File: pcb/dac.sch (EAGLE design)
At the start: 10 parts, among them U1 PIC16F1773-I/SP

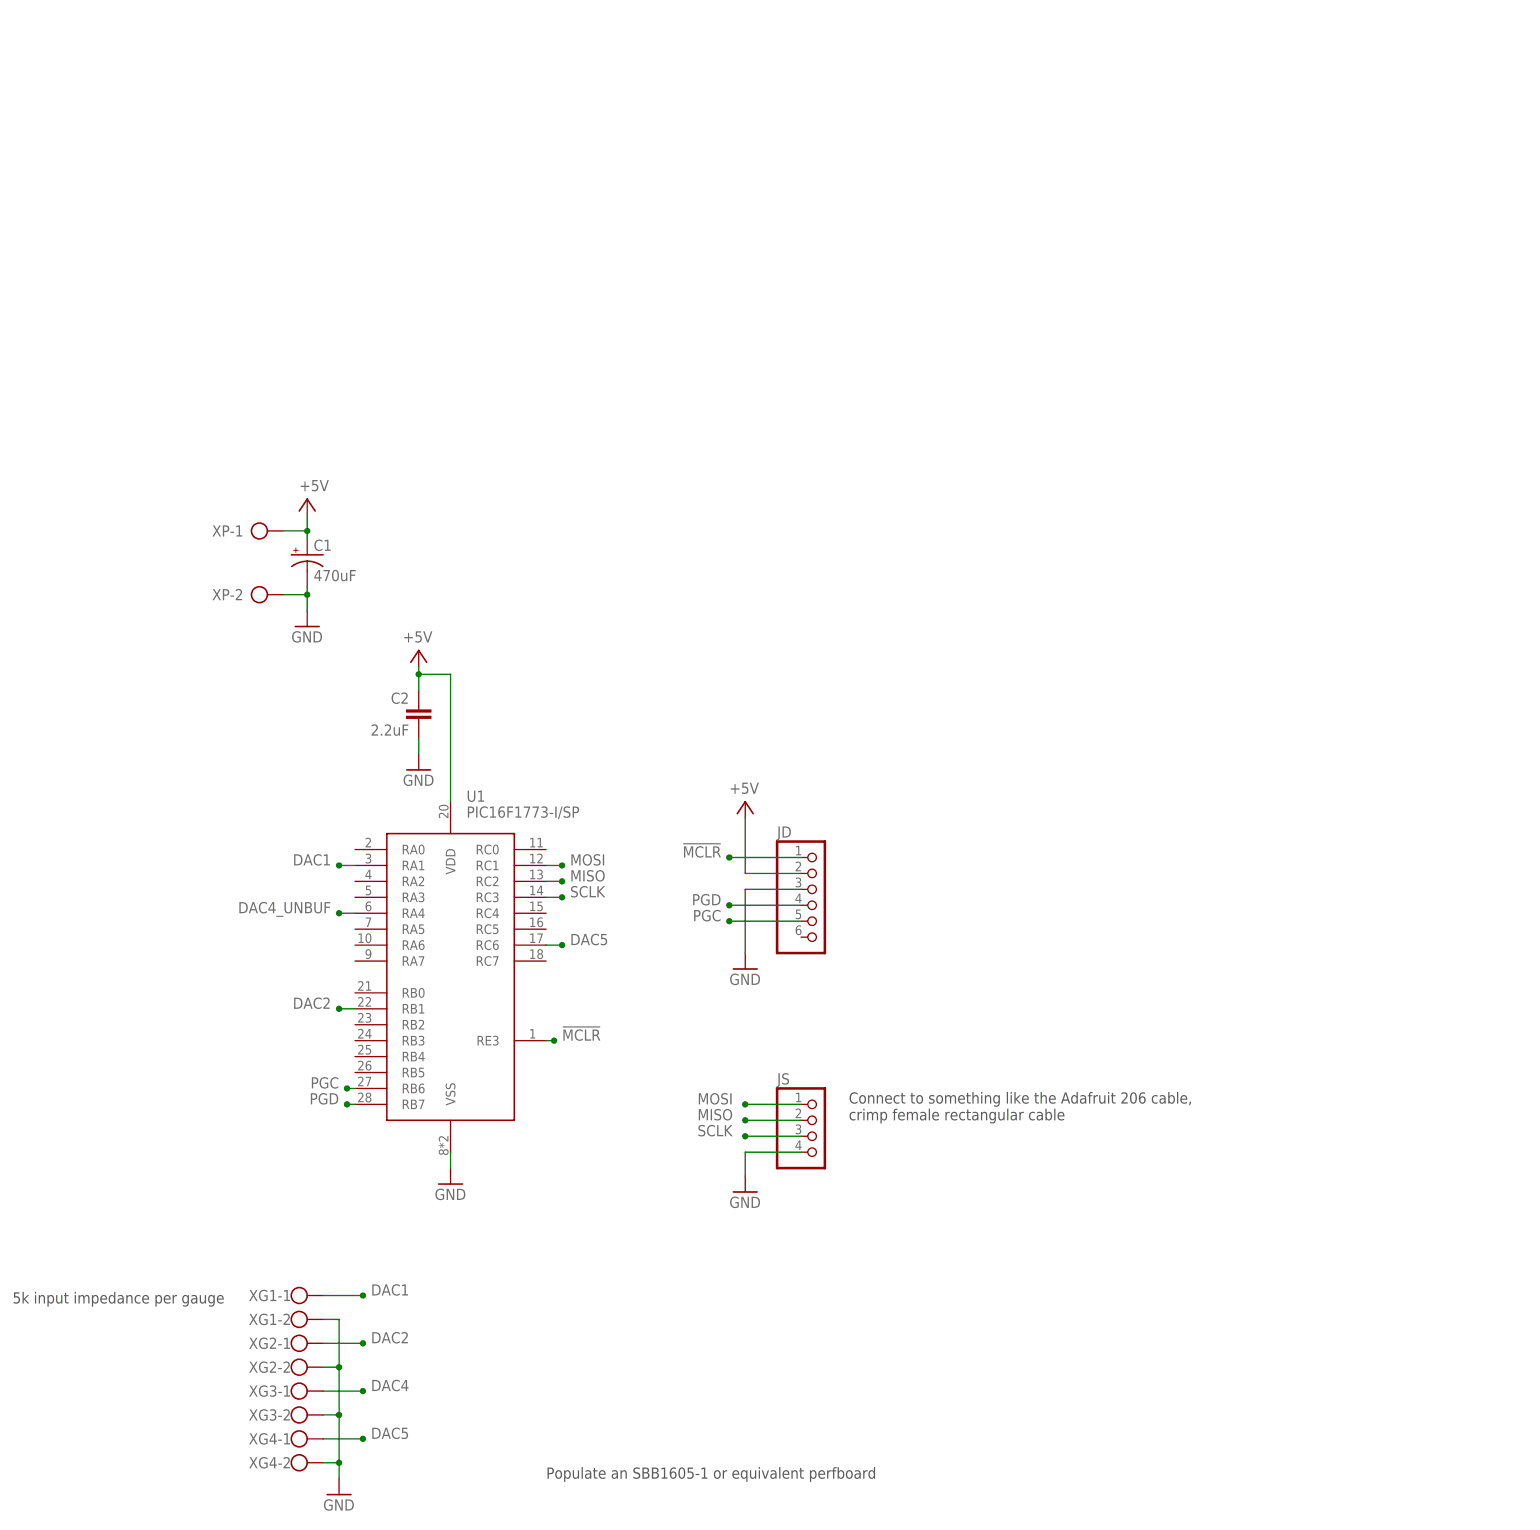
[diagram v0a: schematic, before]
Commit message: Add fade circuit and a little firmware
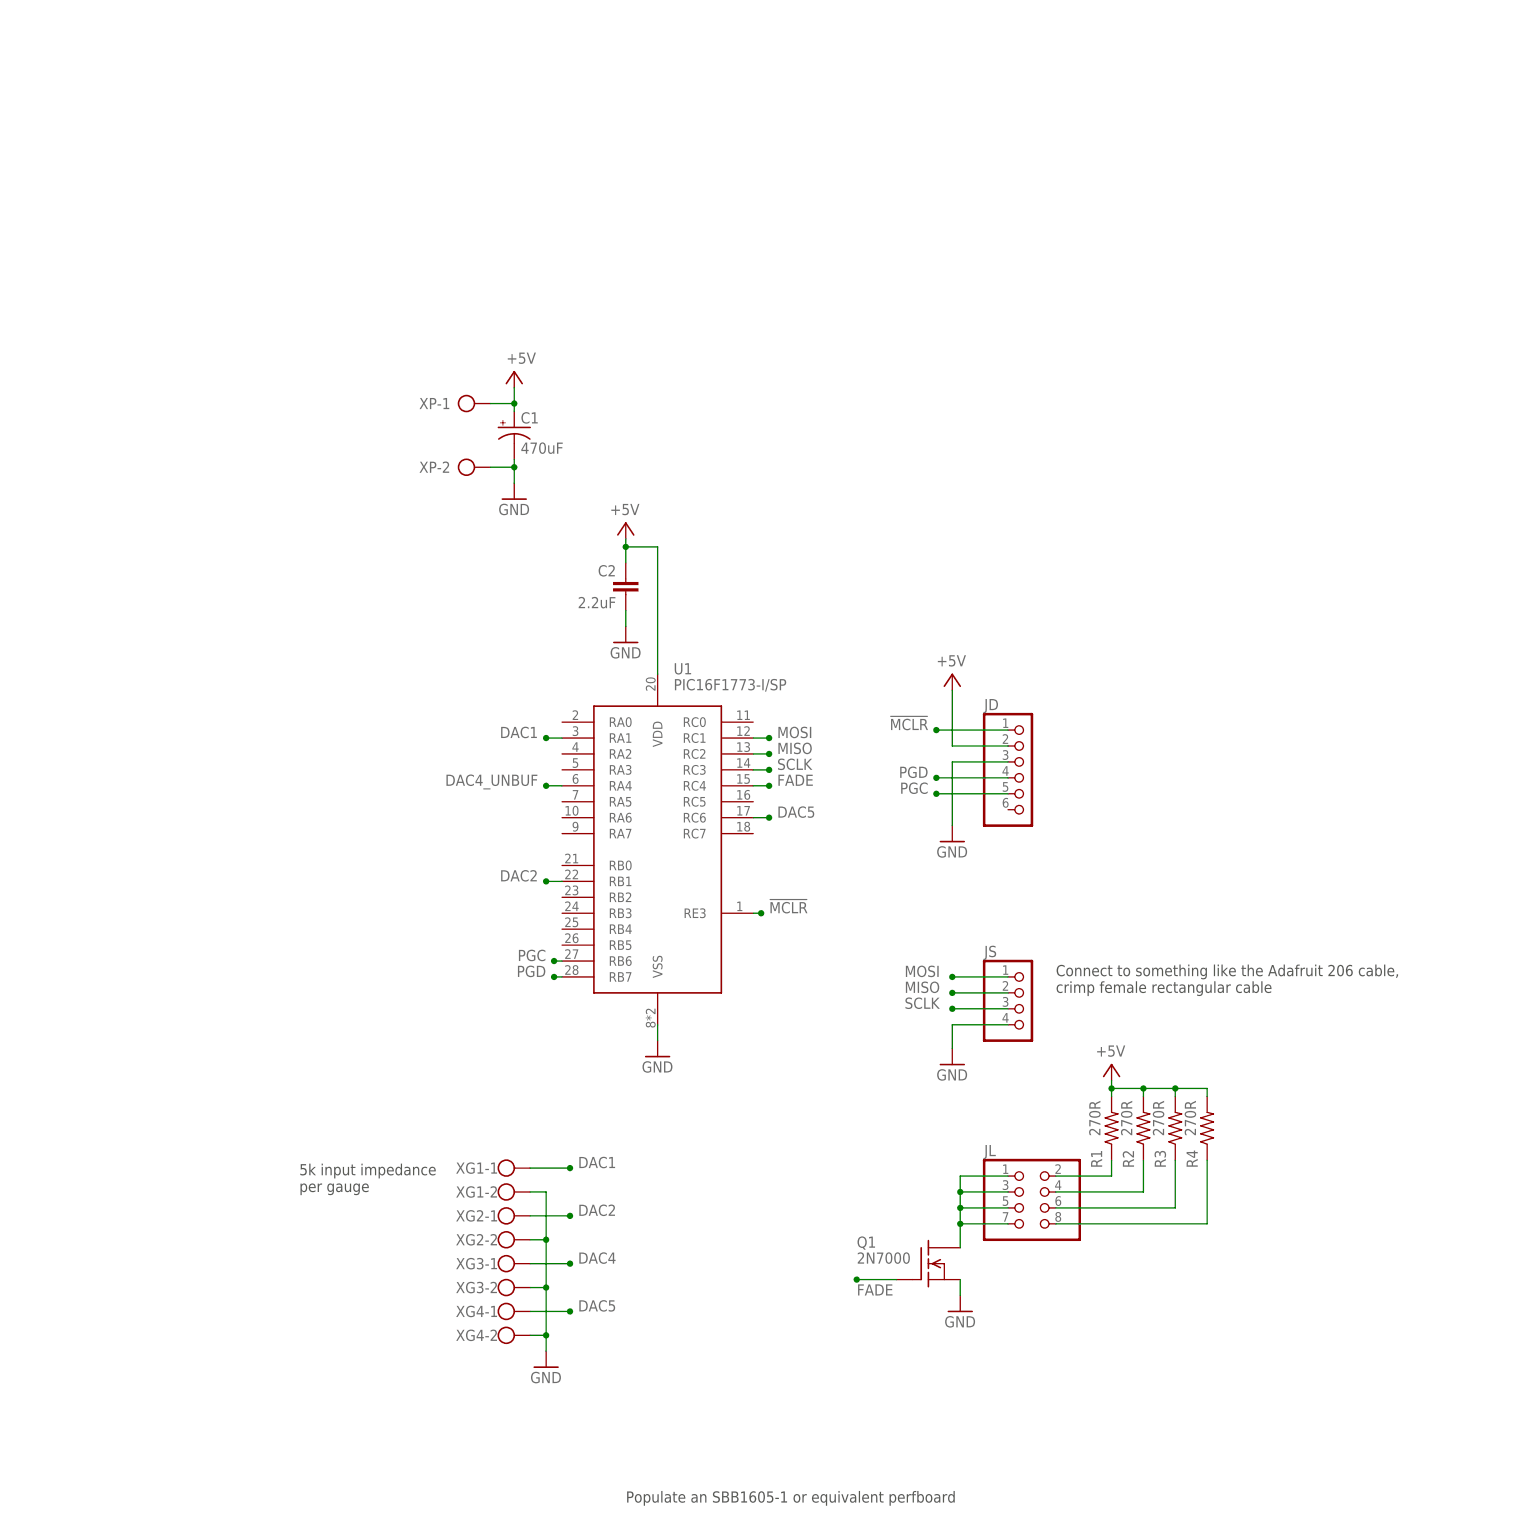
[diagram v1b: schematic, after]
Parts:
- added JL: (no value), pinhead:PINHD-2X4
- added Q1: 2N7000, transistor-fet:TN0604N3
- added R1, R2, R3, R4: 270R, rcl:R-US_0207/7
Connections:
- new net FADE: Q1.G, U1.RC4
- new net LED1: JL.2, R1.1
- new net LED2: JL.4, R2.1
- new net LED3: JL.6, R3.1
- new net LED4: JL.8, R4.1
- new net N$1: JL.1, JL.3, JL.5, JL.7, Q1.D
- net +5V: now also R1.2, R2.2, R3.2, R4.2
- net GND: now also Q1.S
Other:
- moved on the sheet: C1, C2, JD, JS, U1, XG1-1, XG1-2, XG2-1, XG2-2, XG3-1, XG3-2, XG4-1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

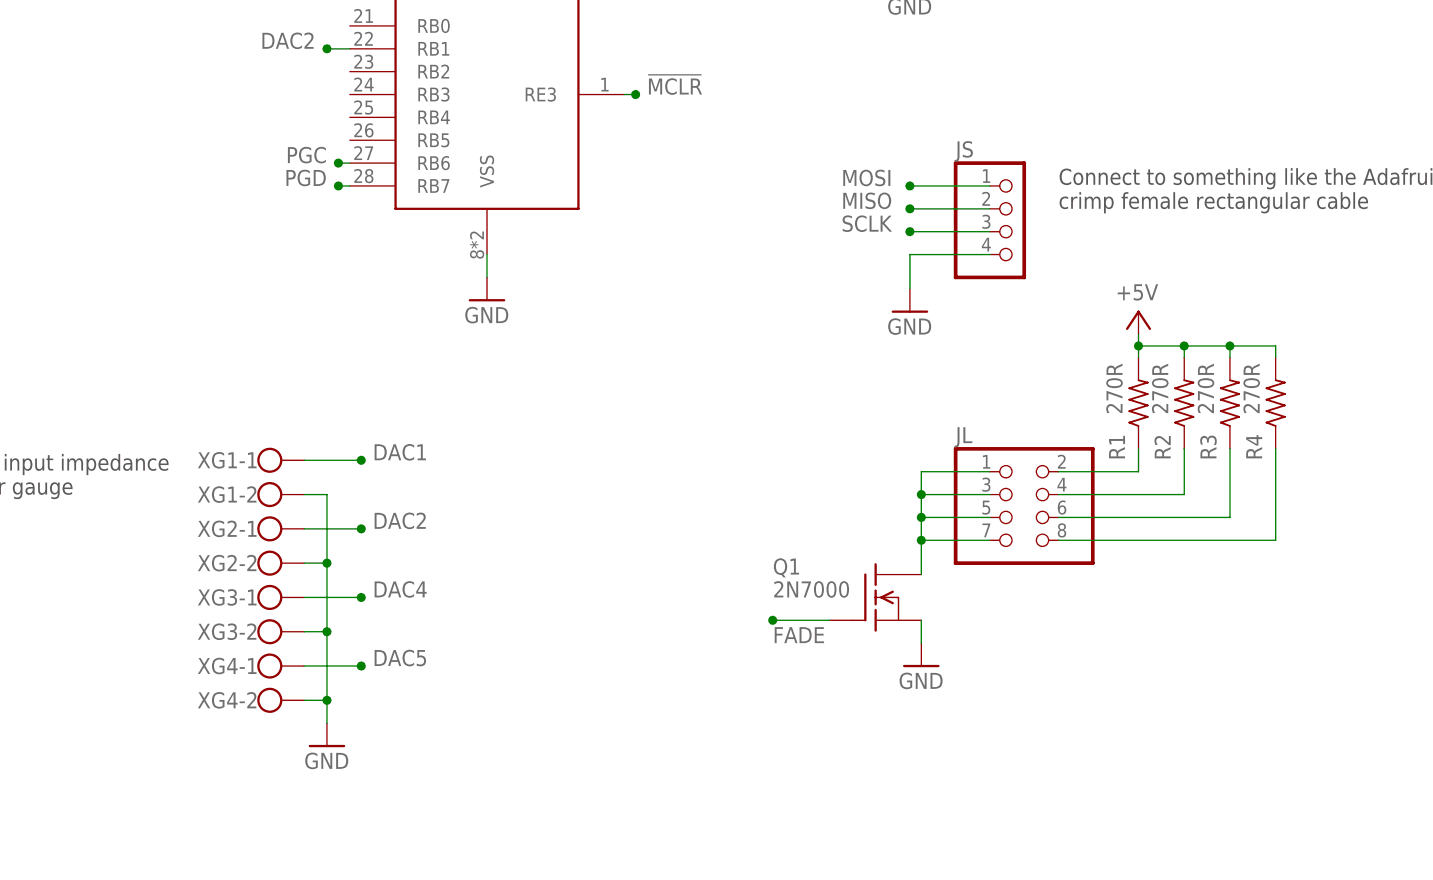
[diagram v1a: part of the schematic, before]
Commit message: Increase LED drive current to 13mA
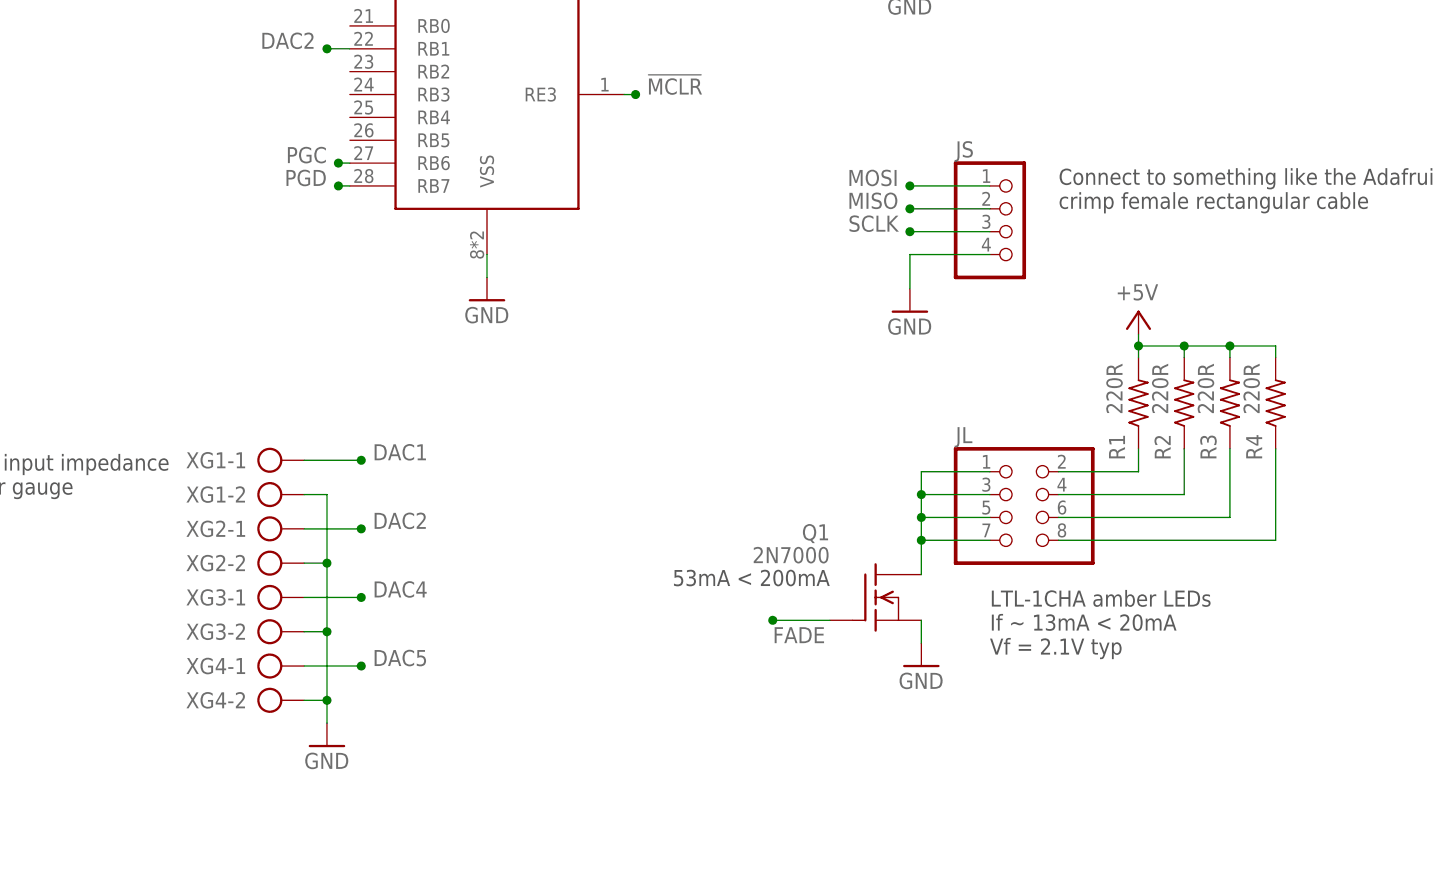
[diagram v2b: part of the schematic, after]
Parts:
- R1, R2, R3, R4: value 270R -> 220R
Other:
- note added: "53mA < 200mA"
- note added: "LTL-1CHA amber LEDs If ~ 13mA < 20mA Vf = 2.1V typ"
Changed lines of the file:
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@@
 <part name="JL" library="pinhead" library_urn="urn:adsk.eagle:library:325" deviceset="PINHD-2X4" device="" package3d_urn="urn:adsk.eagle:package:22461/2"/>
 <part name="P+4" library="supply1" library_urn="urn:adsk.eagle:library:371" deviceset="+5V" device=""/>
-<part name="R1" library="rcl" library_urn="urn:adsk.eagle:library:334" deviceset="R-US_" device="0207/7" package3d_urn="urn:adsk.eagle:package:23493/2" value="270R"/>
-<part name="R2" library="rcl" library_urn="urn:adsk.eagle:library:334" deviceset="R-US_" device="0207/7" package3d_urn="urn:adsk.eagle:package:23493/2" value="270R"/>
-<part name="R3" library="rcl" library_urn="urn:adsk.eagle:library:334" deviceset="R-US_" device="0207/7" package3d_urn="urn:adsk.eagle:package:23493/2" value="270R"/>
-<part name="R4" library="rcl" library_urn="urn:adsk.eagle:library:334" deviceset="R-US_" device="0207/7" package3d_urn="urn:adsk.eagle:package:23493/2" value="270R"/>
+<part name="R1" library="rcl" library_urn="urn:adsk.eagle:library:334" deviceset="R-US_" device="0207/7" package3d_urn="urn:adsk.eagle:package:23493/2" value="220R"/>
+<part name="R2" library="rcl" library_urn="urn:adsk.eagle:library:334" deviceset="R-US_" device="0207/7" package3d_urn="urn:adsk.eagle:package:23493/2" value="220R"/>
+<part name="R3" library="rcl" library_urn="urn:adsk.eagle:library:334" deviceset="R-US_" device="0207/7" package3d_urn="urn:adsk.eagle:package:23493/2" value="220R"/>
+<part name="R4" library="rcl" library_urn="urn:adsk.eagle:library:334" deviceset="R-US_" device="0207/7" package3d_urn="urn:adsk.eagle:package:23493/2" value="220R"/>
 <part name="Q1" library="transistor-fet" library_urn="urn:adsk.eagle:library:396" deviceset="TN0604N3" device="" package3d_urn="urn:adsk.eagle:package:28535/2" value="2N7000"/>
 <part name="GND7" library="supply1" library_urn="urn:adsk.eagle:library:371" deviceset="GND" device=""/>
@@
 <text x="134.62" y="88.9" size="1.778" layer="97">Connect to something like the Adafruit 206 cable,
 crimp female rectangular cable</text>
+<text x="127" y="39.37" size="1.778" layer="97">LTL-1CHA amber LEDs
+If ~ 13mA &lt; 20mA
+Vf = 2.1V typ</text>
+<text x="109.22" y="46.99" size="1.778" layer="97" rot="MR0">53mA &lt; 200mA</text>
 </plain>
 <instances>
@@
 </instance>
 <instance part="XG1" gate="-1" x="45.72" y="60.96" smashed="yes">
-<attribute name="NAME" x="45.72" y="61.849" size="1.778" layer="95" rot="R180"/>
+<attribute name="NAME" x="44.45" y="60.071" size="1.778" layer="95" rot="MR0"/>
 </instance>
 <instance part="XG1" gate="-2" x="45.72" y="57.15" smashed="yes">
 <attribute name="VALUE" x="43.18" y="53.467" size="1.778" layer="96"/>
-<attribute name="NAME" x="45.72" y="58.039" size="1.778" layer="95" rot="R180"/>
+<attribute name="NAME" x="44.45" y="56.261" size="1.778" layer="95" rot="MR0"/>
 </instance>
 <instance part="XG2" gate="-1" x="45.72" y="53.34" smashed="yes">
-<attribute name="NAME" x="45.72" y="54.229" size="1.778" layer="95" rot="R180"/>
+<attribute name="NAME" x="44.45" y="52.451" size="1.778" layer="95" rot="MR0"/>
 </instance>
 <instance part="XG2" gate="-2" x="45.72" y="49.53" smashed="yes">
 <attribute name="VALUE" x="43.18" y="45.847" size="1.778" layer="96"/>
-<attribute name="NAME" x="45.72" y="50.419" size="1.778" layer="95" rot="R180"/>
+<attribute name="NAME" x="44.45" y="48.641" size="1.778" layer="95" rot="MR0"/>
 </instance>
 <instance part="XG3" gate="-1" x="45.72" y="45.72" smashed="yes">
-<attribute name="NAME" x="45.72" y="46.609" size="1.778" layer="95" rot="R180"/>
+<attribute name="NAME" x="44.45" y="44.831" size="1.778" layer="95" rot="MR0"/>
 </instance>
 <instance part="XG3" gate="-2" x="45.72" y="41.91" smashed="yes">
 <attribute name="VALUE" x="43.18" y="38.227" size="1.778" layer="96"/>
-<attribute name="NAME" x="45.72" y="42.799" size="1.778" layer="95" rot="R180"/>
+<attribute name="NAME" x="44.45" y="41.021" size="1.778" layer="95" rot="MR0"/>
 </instance>
 <instance part="XG4" gate="-1" x="45.72" y="38.1" smashed="yes">
-<attribute name="NAME" x="45.72" y="38.989" size="1.778" layer="95" rot="R180"/>
+<attribute name="NAME" x="44.45" y="37.211" size="1.778" layer="95" rot="MR0"/>
 </instance>
 <instance part="XG4" gate="-2" x="45.72" y="34.29" smashed="yes">
 <attribute name="VALUE" x="43.18" y="30.607" size="1.778" layer="96"/>
-<attribute name="NAME" x="45.72" y="35.179" size="1.778" layer="95" rot="R180"/>
+<attribute name="NAME" x="44.45" y="33.401" size="1.778" layer="95" rot="MR0"/>
 </instance>
 <instance part="GND6" gate="1" x="53.34" y="29.21" smashed="yes">
@@
 </instance>
 <instance part="Q1" gate="G$1" x="114.3" y="45.72" smashed="yes">
-<attribute name="VALUE" x="102.87" y="45.72" size="1.778" layer="96"/>
-<attribute name="NAME" x="102.87" y="48.26" size="1.778" layer="95"/>
+<attribute name="VALUE" x="109.22" y="49.53" size="1.778" layer="96" rot="MR0"/>
+<attribute name="NAME" x="109.22" y="52.07" size="1.778" layer="95" rot="MR0"/>
 </instance>
 <instance part="GND7" gate="1" x="119.38" y="38.1" smashed="yes">
@@
 <wire x1="127" y1="91.44" x2="118.11" y2="91.44" width="0.1524" layer="91"/>
 <junction x="118.11" y="91.44"/>
-<label x="110.49" y="91.44" size="1.778" layer="95"/>
+<label x="116.84" y="91.44" size="1.778" layer="95" rot="MR0"/>
 </segment>
 <segment>
@@
 <wire x1="127" y1="88.9" x2="118.11" y2="88.9" width="0.1524" layer="91"/>
 <junction x="118.11" y="88.9"/>
-<label x="110.49" y="88.9" size="1.778" layer="95"/>
+<label x="116.84" y="88.9" size="1.778" layer="95" rot="MR0"/>
 </segment>
 <segment>
@@
 <wire x1="127" y1="86.36" x2="118.11" y2="86.36" width="0.1524" layer="91"/>
 <junction x="118.11" y="86.36"/>
-<label x="110.49" y="86.36" size="1.778" layer="95"/>
-</segment>
-<segment>
+<label x="116.84" y="86.36" size="1.778" layer="95" rot="MR0"/>
+</segment>
+<segment>

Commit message: Protoboard layout & routing
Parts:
- removed JL: (no value), pinhead:PINHD-2X4
- removed XG1, XG2, XG3, XG4: (no value), con-wago-500:W237-102
- added C3: 2.2uF, rcl:C-EU050-024X044
- added D1: SA5.0A, diode:ZENER-DIODEP1-Z12
- added JG1H, JG1L, JG2H, JG2L, JG4H, JG4L, JG5H, JG5L: (no value), pinhead:PINHD-1X1
- added JPH: (no value), pinhead:PINHD-1X4
- added JPL: (no value), pinhead:PINHD-1X3
- added U2: MCP6002-I/P, linear:MCP602P
- R1, R2, R3, R4: device rcl:R-US_0207/7 -> rcl:R-US_0207/2V
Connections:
- removed net N$1: JL.1, JL.3, JL.5, JL.7, Q1.D
- new net DAC1_UNBUF: U1.RA1, U2B.+IN
- new net FADE_L: JPL.1, JPL.2, JPL.3, Q1.D
- net +5V: now also C3.1, D1.C, R1.1, R2.1, R3.1, R4.1, U2P.V+; no longer R1.2, R2.2, R3.2, R4.2
- net DAC1: now also JG1H.1, U2B.-IN, U2B.OUT; no longer U1.RA1, XG1-1.KL
- net DAC2: now also JG2H.1; no longer XG2-1.KL
- net DAC4: now also JG4H.1, U2A.-IN, U2A.OUT; no longer XG3-1.KL
- net DAC4_UNBUF: now also U2A.+IN
- net DAC5: now also JG5H.1; no longer XG4-1.KL
- net GND: now also C3.2, D1.A, JG1L.1, JG2L.1, JG4L.1, JG5L.1, U2P.V-; no longer XG1-2.KL, XG2-2.KL, XG3-2.KL, XG4-2.KL
- net LED1: now also JPH.1, R1.2; no longer JL.2, R1.1
- net LED2: now also JPH.2, R2.2; no longer JL.4, R2.1
- net LED3: now also JPH.3, R3.2; no longer JL.6, R3.1
- net LED4: now also JPH.4, R4.2; no longer JL.8, R4.1
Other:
- moved on the sheet: C1, C2, JD, JS, Q1, R1, R2, R3, R4, U1, XP-1, XP-2
